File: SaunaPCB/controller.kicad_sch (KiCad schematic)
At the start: 11 parts, among them J301 KL2RM5.08, J302 KL2RM5.08, J303 KL2RM5.08, J304 KL2RM5.08, U301 ESP32-DEVKITC

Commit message: some step files added
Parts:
- renumbered J301 to J307, J302 to J308, J303 to J309, J304 to J310, R301 to R314, R302 to R315, R303 to R316, R306 to R317, R304 to R318, R305 to R319, U301 to U306
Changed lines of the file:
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@@
 		(dnp no)
 		(fields_autoplaced yes)
-		(property "Reference" "#PWR0314"
+		(property "Reference" "#PWR0311"
 			(at 46.99 121.92 0)
 			(effects
@@
 			(project "SaunaPCB"
 				(path "/e6d8484d-2bb5-441d-9b2b-e37a9f2fa458/8da01db6-a1a1-4b01-9382-9f6e5fdc0347"
-					(reference "#PWR0314")
+					(reference "#PWR0311")
 					(unit 1)
 				)
@@
 		(on_board yes)
 		(dnp no)
-		(property "Reference" "#PWR0310"
+		(property "Reference" "#PWR0319"
 			(at 200.66 55.88 0)
 			(effects
@@
 			(project "SaunaPCB"
 				(path "/e6d8484d-2bb5-441d-9b2b-e37a9f2fa458/8da01db6-a1a1-4b01-9382-9f6e5fdc0347"
-					(reference "#PWR0310")
+					(reference "#PWR0319")
 					(unit 1)
 				)
@@
 		(on_board yes)
 		(dnp no)
-		(property "Reference" "R306"
+		(property "Reference" "R317"
 			(at 50.8 121.666 90)
 			(effects
@@
 			(project "SaunaPCB"
 				(path "/e6d8484d-2bb5-441d-9b2b-e37a9f2fa458/8da01db6-a1a1-4b01-9382-9f6e5fdc0347"
-					(reference "R306")
+					(reference "R317")
 					(unit 1)
 				)
@@
 		(on_board yes)
 		(dnp no)
-		(property "Reference" "#PWR0309"
+		(property "Reference" "#PWR0317"
 			(at 142.24 88.9 0)
 			(effects
@@
 			(project "SaunaPCB"
 				(path "/e6d8484d-2bb5-441d-9b2b-e37a9f2fa458/8da01db6-a1a1-4b01-9382-9f6e5fdc0347"
-					(reference "#PWR0309")
+					(reference "#PWR0317")
 					(unit 1)
 				)
@@
 		(on_board yes)
 		(dnp no)
-		(property "Reference" "R302"
+		(property "Reference" "R315"
 			(at 50.8 58.166 90)
 			(effects
@@
 			(project "SaunaPCB"
 				(path "/e6d8484d-2bb5-441d-9b2b-e37a9f2fa458/8da01db6-a1a1-4b01-9382-9f6e5fdc0347"
-					(reference "R302")
+					(reference "R315")
 					(unit 1)
 				)
@@
 		(on_board yes)
 		(dnp no)
-		(property "Reference" "J302"
+		(property "Reference" "J308"
 			(at 24.13 65.024 90)
 			(effects
@@
 			(project "SaunaPCB"
 				(path "/e6d8484d-2bb5-441d-9b2b-e37a9f2fa458/8da01db6-a1a1-4b01-9382-9f6e5fdc0347"
-					(reference "J302")
+					(reference "J308")
 					(unit 1)
 				)
@@
 		(on_board yes)
 		(dnp no)
-		(property "Reference" "J304"
+		(property "Reference" "J310"
 			(at 24.13 128.778 90)
 			(effects
@@
 			(project "SaunaPCB"
 				(path "/e6d8484d-2bb5-441d-9b2b-e37a9f2fa458/8da01db6-a1a1-4b01-9382-9f6e5fdc0347"
-					(reference "J304")
+					(reference "J310")
 					(unit 1)
 				)
@@
 		(dnp no)
 		(fields_autoplaced yes)
-		(property "Reference" "#PWR0301"
+		(property "Reference" "#PWR0308"
 			(at 46.99 26.67 0)
 			(effects
@@
 			(project "SaunaPCB"
 				(path "/e6d8484d-2bb5-441d-9b2b-e37a9f2fa458/8da01db6-a1a1-4b01-9382-9f6e5fdc0347"
-					(reference "#PWR0301")
+					(reference "#PWR0308")
 					(unit 1)
 				)
@@
 		(dnp no)
 		(fields_autoplaced yes)
-		(property "Reference" "#PWR0303"
+		(property "Reference" "#PWR0310"
 			(at 46.99 90.17 0)
 			(effects
@@
 			(project "SaunaPCB"
 				(path "/e6d8484d-2bb5-441d-9b2b-e37a9f2fa458/8da01db6-a1a1-4b01-9382-9f6e5fdc0347"
-					(reference "#PWR0303")
+					(reference "#PWR0310")
 					(unit 1)
 				)
@@
 		(dnp no)
 		(fields_autoplaced yes)
-		(property "Reference" "#PWR0302"
+		(property "Reference" "#PWR0309"
 			(at 46.99 58.42 0)
 			(effects
@@
 			(project "SaunaPCB"
 				(path "/e6d8484d-2bb5-441d-9b2b-e37a9f2fa458/8da01db6-a1a1-4b01-9382-9f6e5fdc0347"
-					(reference "#PWR0302")
+					(reference "#PWR0309")
 					(unit 1)
 				)
@@
 		(on_board yes)
 		(dnp no)
-		(property "Reference" "R301"
+		(property "Reference" "R314"
 			(at 50.8 26.416 90)
 			(effects
@@
 			(project "SaunaPCB"
 				(path "/e6d8484d-2bb5-441d-9b2b-e37a9f2fa458/8da01db6-a1a1-4b01-9382-9f6e5fdc0347"
-					(reference "R301")
+					(reference "R314")
 					(unit 1)
 				)
@@
 		(on_board yes)
 		(dnp no)
-		(property "Reference" "R304"
+		(property "Reference" "R318"
 			(at 204.47 44.196 90)
 			(effects
@@
 			(project "SaunaPCB"
 				(path "/e6d8484d-2bb5-441d-9b2b-e37a9f2fa458/8da01db6-a1a1-4b01-9382-9f6e5fdc0347"
-					(reference "R304")
+					(reference "R318")
 					(unit 1)
 				)
@@
 		(dnp no)
 		(fields_autoplaced yes)
-		(property "Reference" "#FLG0301"
+		(property "Reference" "#FLG0304"
 			(at 149.86 52.705 0)
 			(effects
@@
 			(project ""
 				(path "/e6d8484d-2bb5-441d-9b2b-e37a9f2fa458/8da01db6-a1a1-4b01-9382-9f6e5fdc0347"
-					(reference "#FLG0301")
+					(reference "#FLG0304")
 					(unit 1)
 				)
@@
 		(on_board yes)
 		(dnp no)
-		(property "Reference" "#PWR0305"
+		(property "Reference" "#PWR0313"
 			(at 52.07 76.2 0)
 			(effects
@@
 			(project "SaunaPCB"
 				(path "/e6d8484d-2bb5-441d-9b2b-e37a9f2fa458/8da01db6-a1a1-4b01-9382-9f6e5fdc0347"
-					(reference "#PWR0305")
+					(reference "#PWR0313")
 					(unit 1)
 				)
@@
 		(on_board yes)
 		(dnp no)
-		(property "Reference" "R303"
+		(property "Reference" "R316"
 			(at 50.8 89.916 90)
 			(effects
@@
 			(project "SaunaPCB"
 				(path "/e6d8484d-2bb5-441d-9b2b-e37a9f2fa458/8da01db6-a1a1-4b01-9382-9f6e5fdc0347"
-					(reference "R303")
+					(reference "R316")
 					(unit 1)
 				)
@@
 		(on_board yes)
 		(dnp no)
-		(property "Reference" "#PWR0304"
+		(property "Reference" "#PWR0312"
 			(at 52.07 44.45 0)
 			(effects
@@
 			(project "SaunaPCB"
 				(path "/e6d8484d-2bb5-441d-9b2b-e37a9f2fa458/8da01db6-a1a1-4b01-9382-9f6e5fdc0347"
-					(reference "#PWR0304")
+					(reference "#PWR0312")
 					(unit 1)
 				)
@@
 		(on_board yes)
 		(dnp no)
-		(property "Reference" "J301"
+		(property "Reference" "J307"
 			(at 24.13 33.528 90)
 			(effects
@@
 			(project "SaunaPCB"
 				(path "/e6d8484d-2bb5-441d-9b2b-e37a9f2fa458/8da01db6-a1a1-4b01-9382-9f6e5fdc0347"
-					(reference "J301")
+					(reference "J307")
 					(unit 1)
 				)
@@
 		(dnp no)
 		(fields_autoplaced yes)
-		(property "Reference" "#PWR0311"
+		(property "Reference" "#PWR0320"
 			(at 200.66 71.12 0)
 			(effects
@@
 			(project "SaunaPCB"
 				(path "/e6d8484d-2bb5-441d-9b2b-e37a9f2fa458/8da01db6-a1a1-4b01-9382-9f6e5fdc0347"
-					(reference "#PWR0311")
+					(reference "#PWR0320")
 					(unit 1)
 				)
@@
 		(on_board yes)
 		(dnp no)
-		(property "Reference" "J303"
+		(property "Reference" "J309"
 			(at 24.13 97.028 90)
 			(effects
@@
 			(project "SaunaPCB"
 				(path "/e6d8484d-2bb5-441d-9b2b-e37a9f2fa458/8da01db6-a1a1-4b01-9382-9f6e5fdc0347"
-					(reference "J303")
+					(reference "J309")
 					(unit 1)
 				)
@@
 		(dnp no)
 		(fields_autoplaced yes)
-		(property "Reference" "#PWR0308"
+		(property "Reference" "#PWR0316"
 			(at 152.4 55.88 0)
 			(effects
@@
 			(project ""
 				(path "/e6d8484d-2bb5-441d-9b2b-e37a9f2fa458/8da01db6-a1a1-4b01-9382-9f6e5fdc0347"
-					(reference "#PWR0308")
+					(reference "#PWR0316")
 					(unit 1)
 				)
@@
 		(dnp no)
 		(fields_autoplaced yes)
-		(property "Reference" "#PWR0307"
+		(property "Reference" "#PWR0318"
 			(at 152.4 101.6 0)
 			(effects
@@
 			(project "SaunaPCB"
 				(path "/e6d8484d-2bb5-441d-9b2b-e37a9f2fa458/8da01db6-a1a1-4b01-9382-9f6e5fdc0347"
-					(reference "#PWR0307")
+					(reference "#PWR0318")
 					(unit 1)
 				)
@@
 		(dnp no)
 		(fields_autoplaced yes)
-		(property "Reference" "#PWR0313"
+		(property "Reference" "#PWR0322"
 			(at 209.55 44.45 0)
 			(effects
@@
 			(project "SaunaPCB"
 				(path "/e6d8484d-2bb5-441d-9b2b-e37a9f2fa458/8da01db6-a1a1-4b01-9382-9f6e5fdc0347"
-					(reference "#PWR0313")
+					(reference "#PWR0322")
 					(unit 1)
 				)
@@
 		(on_board yes)
 		(dnp no)
-		(property "Reference" "#PWR0306"
+		(property "Reference" "#PWR0314"
 			(at 52.07 107.95 0)
 			(effects
@@
 			(project "SaunaPCB"
 				(path "/e6d8484d-2bb5-441d-9b2b-e37a9f2fa458/8da01db6-a1a1-4b01-9382-9f6e5fdc0347"
-					(reference "#PWR0306")
+					(reference "#PWR0314")
 					(unit 1)
 				)
@@
 		(dnp no)
 		(fields_autoplaced yes)
-		(property "Reference" "U301"
+		(property "Reference" "U306"
 			(at 172.72 48.26 0)
 			(effects
@@
 			(project ""
 				(path "/e6d8484d-2bb5-441d-9b2b-e37a9f2fa458/8da01db6-a1a1-4b01-9382-9f6e5fdc0347"
-					(reference "U301")
+					(reference "U306")
 					(unit 1)
 				)
@@
 		(on_board yes)
 		(dnp no)
-		(property "Reference" "R305"
+		(property "Reference" "R319"
 			(at 213.36 44.196 90)
 			(effects
@@
 			(project "SaunaPCB"
 				(path "/e6d8484d-2bb5-441d-9b2b-e37a9f2fa458/8da01db6-a1a1-4b01-9382-9f6e5fdc0347"
-					(reference "R305")
+					(reference "R319")
 					(unit 1)
 				)
@@
 		(dnp no)
 		(fields_autoplaced yes)
-		(property "Reference" "#PWR0312"
+		(property "Reference" "#PWR0321"
 			(at 200.66 44.45 0)
 			(effects
@@
 			(project "SaunaPCB"
 				(path "/e6d8484d-2bb5-441d-9b2b-e37a9f2fa458/8da01db6-a1a1-4b01-9382-9f6e5fdc0347"
-					(reference "#PWR0312")
-					(unit 1)
-				)
+					(reference "#PWR0321")
+					(unit 1)
+				)

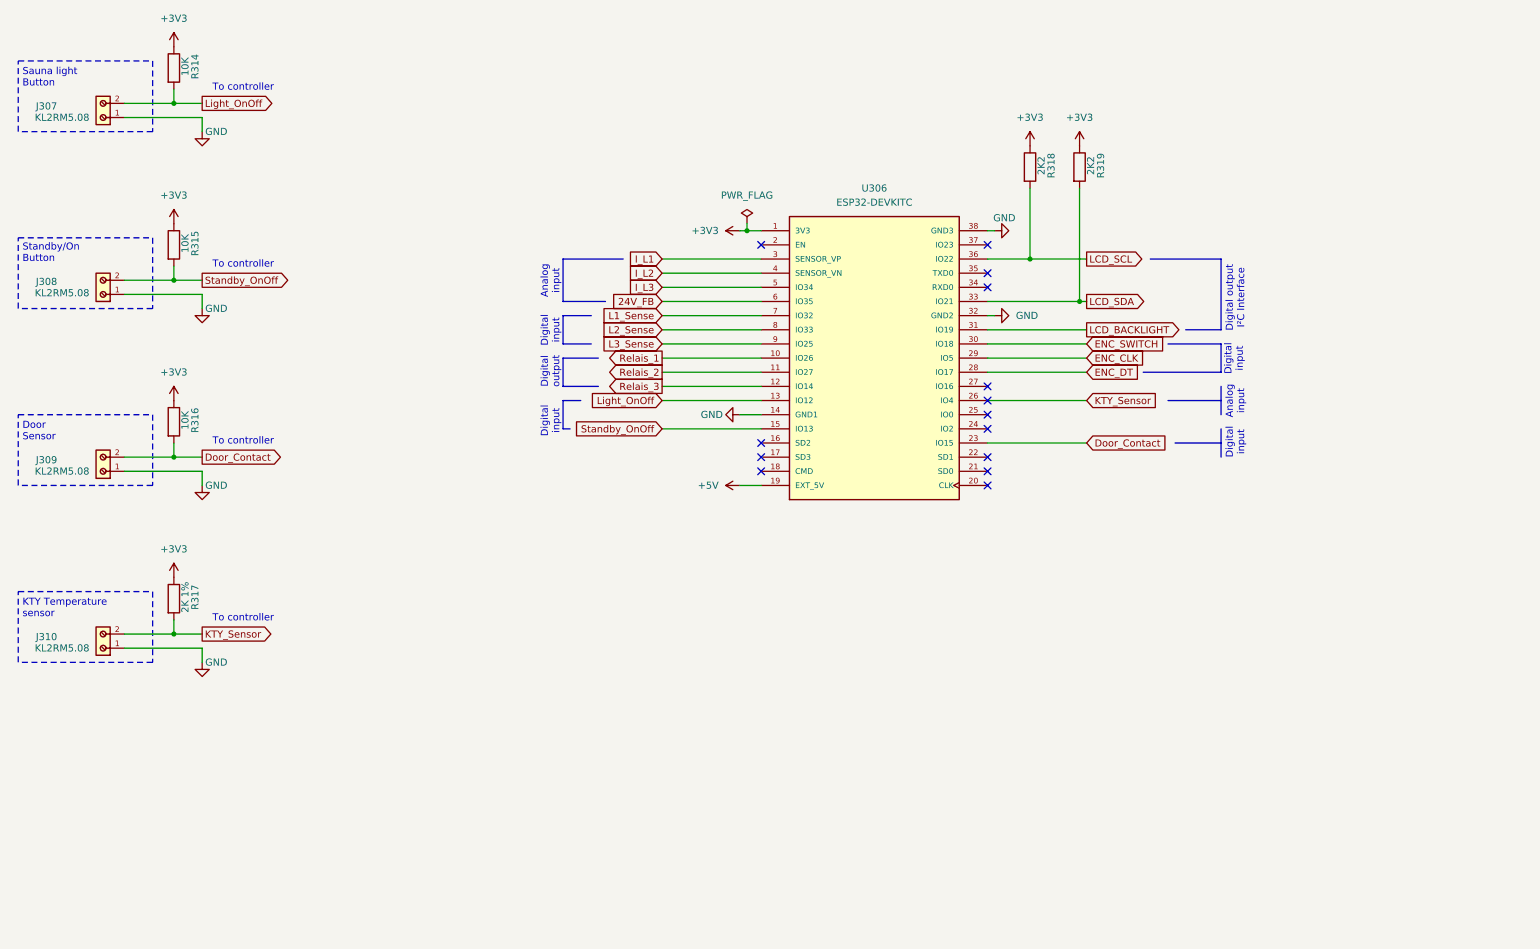
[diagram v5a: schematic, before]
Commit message: Hall sensors for current measurement added
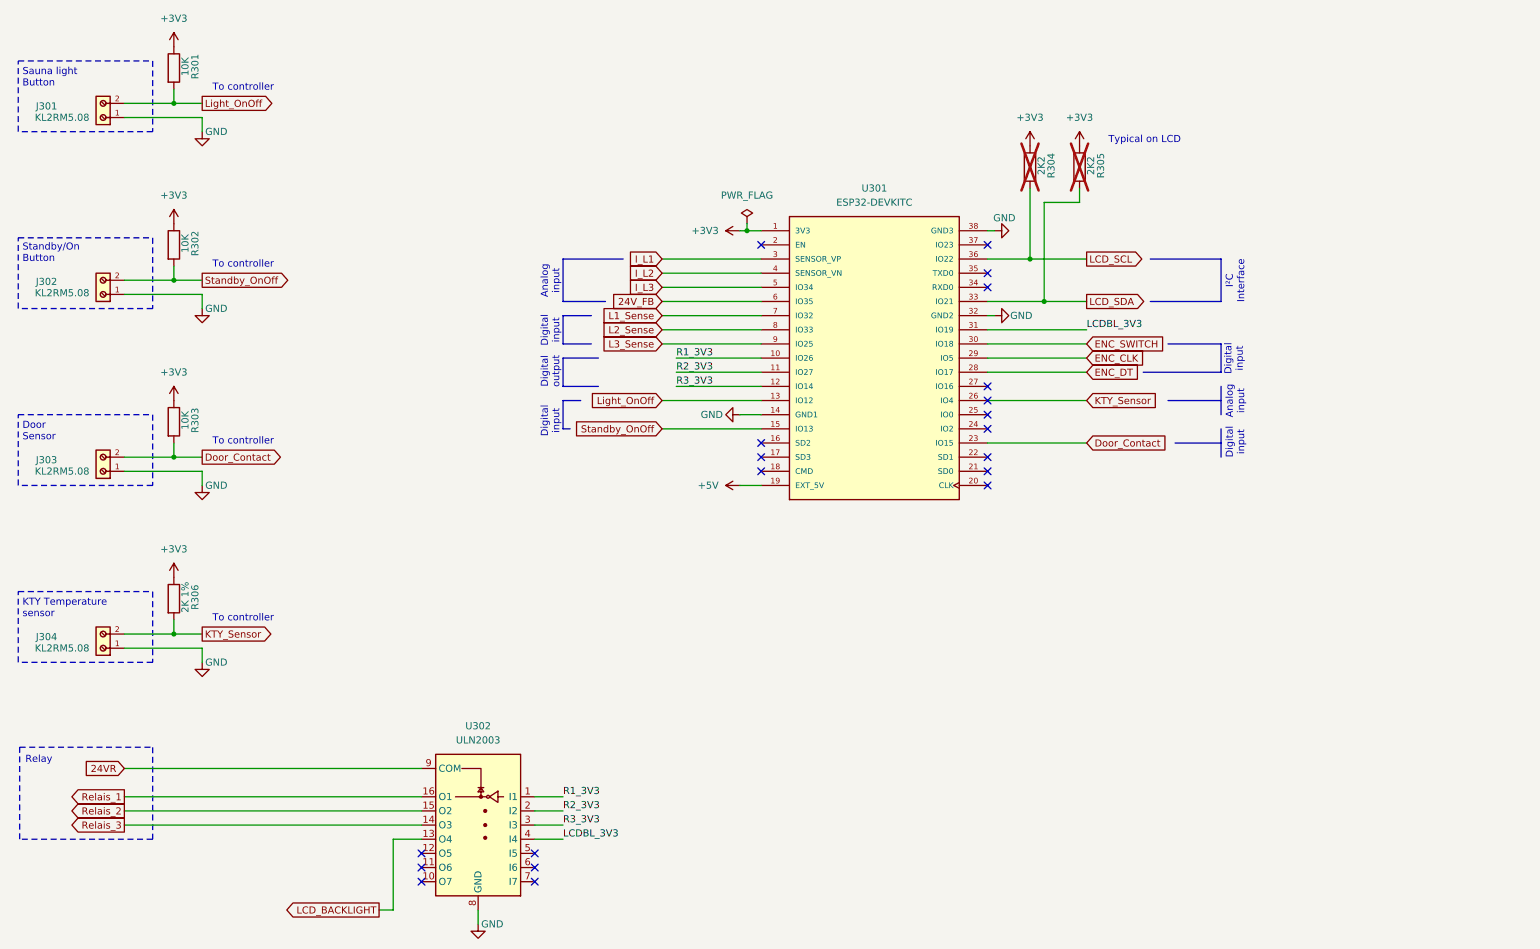
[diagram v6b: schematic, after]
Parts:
- added U302: ULN2003, Package_DIP:DIP-16_W7.62mm, symbol Transistor_Array:ULN2003
- R304: renamed from R318; now not fitted
- R305: renamed from R319; now not fitted
- renumbered J307 to J301, J308 to J302, J309 to J303, J310 to J304, R314 to R301, R315 to R302, R316 to R303, R317 to R306, U306 to U301
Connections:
- net GND: now also U302.8 (GND)
- net LCD_BACKLIGHT: now also U302.13 (O4); no longer U301.31 (IO19)
- net Relais_1: now also U302.16 (O1); no longer U301.10 (IO26)
- net Relais_2: now also U302.15 (O2); no longer U301.11 (IO27)
- net Relais_3: now also U302.14 (O3); no longer U301.12 (IO14)
- new net 24VR: U302.9 (COM)
- new net LCDBL_3V3: U301.31 (IO19), U302.4 (I4)
- new net R1_3V3: U301.10 (IO26), U302.1 (I1)
- new net R2_3V3: U301.11 (IO27), U302.2 (I2)
- new net R3_3V3: U301.12 (IO14), U302.3 (I3)
- no-connect marks 14 -> 20
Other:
- note added: "I²C Interface"
- note added: "Relay"
- note added: "Typical on LCD"
- note removed: "Digital output I²C Interface"

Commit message: Connector to LCD and decoder added
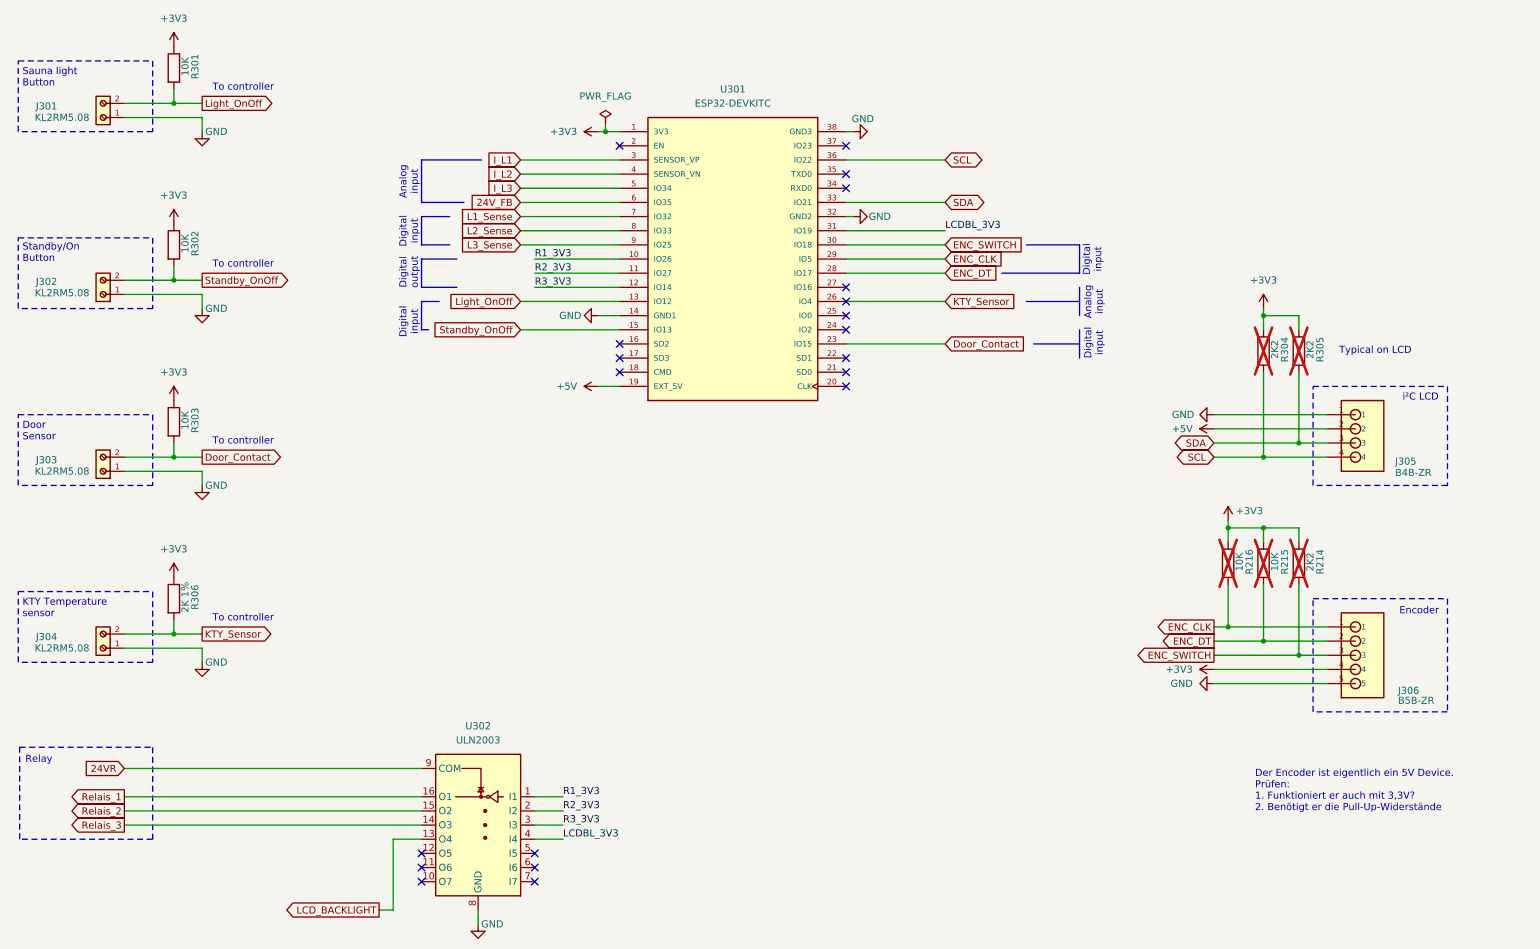
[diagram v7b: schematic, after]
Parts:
- added J305: B4B-ZR, MyConnectors:B4B-ZR, symbol MyConnectors:B4B-ZR
- added J306: B5B-ZR, MyConnectors:B5B-ZR, symbol MyConnectors:B5B-ZR
- added R214: 2K2, Resistor_SMD:R_1206_3216Metric, symbol Device:R
- added R215, R216: 10K, Resistor_SMD:R_1206_3216Metric, symbol Device:R
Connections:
- net +3V3: now also J306.4, R214.1, R215.1, R216.1
- net +5V: now also J305.2
- net ENC_CLK: now also J306.1, R216.2
- net ENC_DT: now also J306.2, R215.2
- net ENC_SWITCH: now also J306.3, R214.2
- net GND: now also J305.1, J306.5
- net LCD_SCL renamed SCL
- net SCL: now also J305.4
- net LCD_SDA renamed SDA
- net SDA: now also J305.3
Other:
- note added: "Der Encoder ist eigentlich ein 5V Device. Prüfen: 1. Funktioniert er auch mit 3,3V? 2. Benötigt er die Pull-Up-Widerstände"
- note added: "Encoder"
- note added: "i²C LCD"
- note removed: "I²C Interface"
- moved on the sheet: R304, R305, U301
